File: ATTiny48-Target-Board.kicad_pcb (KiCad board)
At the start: 2 copper layers, 25.4 x 50.8 mm, 11 parts, among them J1 Conn_01x14_Pin, J2 Conn_01x14_Pin, U1 ATtiny48-P

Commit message: v1.0 ready to be paneled and sent to fab
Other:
- board text added: "/RST"
- board text added: "AVCC"
- board text added: "GND"
- board text added: "MISO"
- board text added: "MOSI"
- board text added: "PB0"
- board text added: "PB1"
- board text added: "PB2"
- board text added: "PB6"
- board text added: "PB7"
- board text added: "PC0"
- board text added: "PC1"
- board text added: "PC2"
- board text added: "PC3"
- board text added: "PC7"
- board text added: "PD0"
- board text added: "PD1"
- board text added: "PD2"
- board text added: "PD3"
- board text added: "PD4"
- board text added: "PD5"
- board text added: "RX"
- board text added: "SCK"
- board text added: "SCL"
- board text added: "SDA"
- board text added: "TX"
- board text added: "VCC"
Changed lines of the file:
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@@
     (title "ATtiny48 Target Board")
     (date "2023-06-13")
-    (rev "v0.4")
+    (rev "v1.0")
+    (comment 1 "Bare Bones MicroController for ATtiny48 & ATtiny88")
+    (comment 2 "BBMC-T48/T88")
   )
   (layers
@@
   (gr_rect (start 107.95 44.196) (end 133.35 94.996)
     (stroke (width 0.15) (type default)) (fill none) (layer "Edge.Cuts"))
-  (gr_text "BBMC-T48/T88\nV1.0   N7TDB" (at 114.808 57.404 90) (layer "F.SilkS")
-    (effects (font (size 1 1) (thickness 0.15)) (justify left bottom))
-  )
+  (gr_text "GND" (at 127.254 60.96) (layer "F.SilkS")
+    (effects (font (size 1 1) (thickness 0.15)) (justify left bottom))
+  )
+  (gr_text "BBMC-T48/T88\nV1.0   N7TDB" (at 115.57 94.234 90) (layer "F.SilkS")
+    (effects (font (size 0.8 0.7) (thickness 0.125)) (justify left bottom))
+  )
+  (gr_text "PB6" (at 110.744 66.04) (layer "F.SilkS")
+    (effects (font (size 1 1) (thickness 0.15)) (justify left bottom))
+  )
+  (gr_text "PC0" (at 127.254 58.42) (layer "F.SilkS")
+    (effects (font (size 1 1) (thickness 0.15)) (justify left bottom))
+  )
+  (gr_text "SCK" (at 127.254 68.58) (layer "F.SilkS")
+    (effects (font (size 1 1) (thickness 0.15)) (justify left bottom))
+  )
+  (gr_text "PB1" (at 127.254 78.74) (layer "F.SilkS")
+    (effects (font (size 1 1) (thickness 0.15)) (justify left bottom))
+  )
+  (gr_text "PC3" (at 127.254 50.8) (layer "F.SilkS")
+    (effects (font (size 1 1) (thickness 0.15)) (justify left bottom))
+  )
+  (gr_text "AVCC" (at 126.492 66.04) (layer "F.SilkS")
+    (effects (font (size 1 1) (thickness 0.15)) (justify left bottom))
+  )
+  (gr_text "GND" (at 110.55 63.53) (layer "F.SilkS")
+    (effects (font (size 1 1) (thickness 0.15)) (justify left bottom))
+  )
+  (gr_text "SDA" (at 127.254 48.26) (layer "F.SilkS")
+    (effects (font (size 1 1) (thickness 0.15)) (justify left bottom))
+  )
+  (gr_text "PB2" (at 127.254 76.2) (layer "F.SilkS")
+    (effects (font (size 1 1) (thickness 0.15)) (justify left bottom))
+  )
+  (gr_text "TX" (at 110.744 73.66) (layer "F.SilkS")
+    (effects (font (size 1 1) (thickness 0.15)) (justify left bottom))
+  )
+  (gr_text "PD4" (at 110.744 58.42) (layer "F.SilkS")
+    (effects (font (size 1 1) (thickness 0.15)) (justify left bottom))
+  )
+  (gr_text "PB0" (at 110.744 78.74) (layer "F.SilkS")
+    (effects (font (size 1 1) (thickness 0.15)) (justify left bottom))
+  )
+  (gr_text "PC2" (at 127.254 53.34) (layer "F.SilkS")
+    (effects (font (size 1 1) (thickness 0.15)) (justify left bottom))
+  )
+  (gr_text "PD3" (at 110.744 55.88) (layer "F.SilkS")
+    (effects (font (size 1 1) (thickness 0.15)) (justify left bottom))
+  )
+  (gr_text "PB7" (at 110.744 68.58) (layer "F.SilkS")
+    (effects (font (size 1 1) (thickness 0.15)) (justify left bottom))
+  )
+  (gr_text "MOSI" (at 126.746 73.66) (layer "F.SilkS")
+    (effects (font (size 1 1) (thickness 0.15)) (justify left bottom))
+  )
+  (gr_text "PD0" (at 110.744 48.26) (layer "F.SilkS")
+    (effects (font (size 1 1) (thickness 0.15)) (justify left bottom))
+  )
+  (gr_text "PD1" (at 110.744 50.8) (layer "F.SilkS")
+    (effects (font (size 1 1) (thickness 0.15)) (justify left bottom))
+  )
+  (gr_text "PC7" (at 127.254 63.754) (layer "F.SilkS")
+    (effects (font (size 1 1) (thickness 0.15)) (justify left bottom))
+  )
+  (gr_text "PD5" (at 110.744 71.12) (layer "F.SilkS")
+    (effects (font (size 1 1) (thickness 0.15)) (justify left bottom))
+  )
+  (gr_text "RX" (at 110.744 76.2) (layer "F.SilkS")
+    (effects (font (size 1 1) (thickness 0.15)) (justify left bottom))
+  )
+  (gr_text "VCC" (at 110.744 60.96) (layer "F.SilkS")
+    (effects (font (size 1 1) (thickness 0.15)) (justify left bottom))
+  )
+  (gr_text "/RST" (at 110.744 45.72) (layer "F.SilkS")
+    (effects (font (size 1 1) (thickness 0.15)) (justify left bottom))
+  )
+  (gr_text "PC1" (at 127.254 55.88) (layer "F.SilkS")
+    (effects (font (size 1 1) (thickness 0.15)) (justify left bottom))
+  )
+  (gr_text "PD2" (at 110.744 53.34) (layer "F.SilkS")
+    (effects (font (size 1 1) (thickness 0.15)) (justify left bottom))
+  )
+  (gr_text "SCL" (at 127.254 45.72) (layer "F.SilkS")
+    (effects (font (size 1 1) (thickness 0.15)) (justify left bottom))
+  )
+  (gr_text "MISO" (at 126.746 71.12) (layer "F.SilkS")
+    (effects (font (size 1 1) (thickness 0.15)) (justify left bottom))
+  )

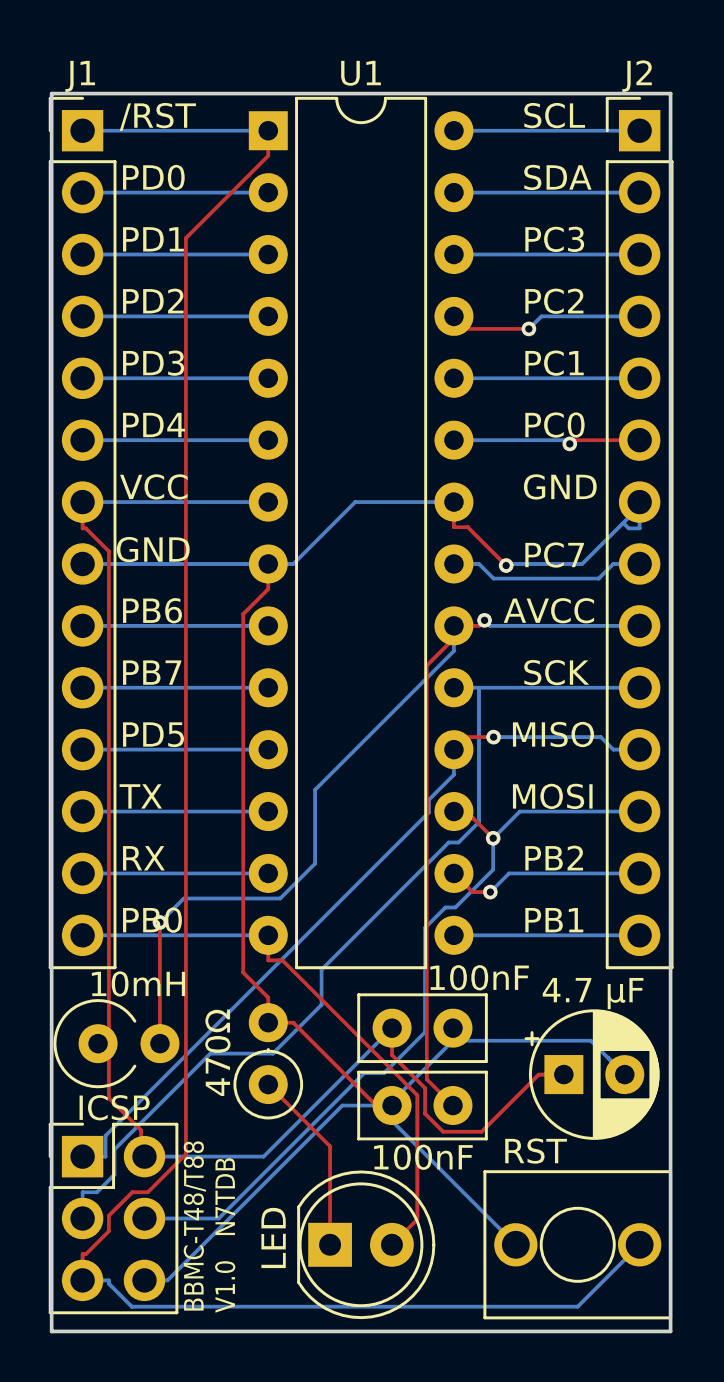
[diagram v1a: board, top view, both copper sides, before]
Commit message: v1.1 change hinky trace on pin 22
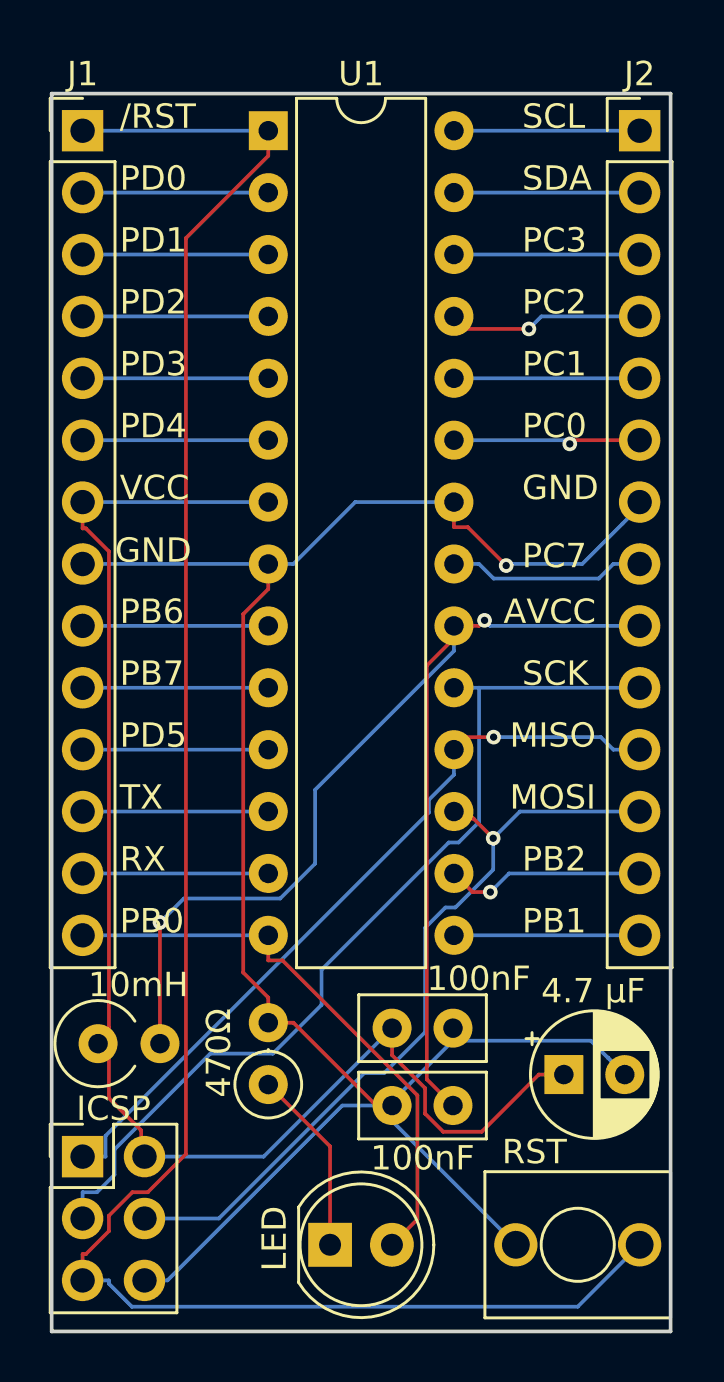
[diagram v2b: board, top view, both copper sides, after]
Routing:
- net GND: track 88.0 -> 86.1 mm
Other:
- board text added: "BBMC-T48/T88 V1.1 N7TDB"
- board text removed: "BBMC-T48/T88 V1.0 N7TDB"
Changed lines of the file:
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@@
   (title_block
     (title "ATtiny48 Target Board")
-    (date "2023-06-13")
-    (rev "v1.0")
+    (date "2023-06-14")
+    (rev "v1.1")
     (comment 1 "Bare Bones MicroController for ATtiny48 & ATtiny88")
     (comment 2 "BBMC-T48/T88")
@@
   )
   (setup
+    (stackup
+      (layer "F.SilkS" (type "Top Silk Screen"))
+      (layer "F.Paste" (type "Top Solder Paste"))
+      (layer "F.Mask" (type "Top Solder Mask") (thickness 0.01))
+      (layer "F.Cu" (type "copper") (thickness 0.035))
+      (layer "dielectric 1" (type "core") (thickness 1.51) (material "FR4") (epsilon_r 4.5) (loss_tangent 0.02))
+      (layer "B.Cu" (type "copper") (thickness 0.035))
+      (layer "B.Mask" (type "Bottom Solder Mask") (thickness 0.01))
+      (layer "B.Paste" (type "Bottom Solder Paste"))
+      (layer "B.SilkS" (type "Bottom Silk Screen"))
+      (copper_finish "None")
+      (dielectric_constraints no)
+    )
     (pad_to_mask_clearance 0.0508)
     (solder_mask_min_width 0.25)
@@
   (gr_rect (start 107.95 44.196) (end 133.35 94.996)
     (stroke (width 0.15) (type default)) (fill none) (layer "Edge.Cuts"))
+  (gr_text "BBMC-T48/T88\nV1.1   N7TDB" (at 114.808 46.99 90) (layer "B.SilkS")
+    (effects (font (size 1 1) (thickness 0.125)) (justify left bottom mirror))
+  )
   (gr_text "GND" (at 127.254 60.96) (layer "F.SilkS")
     (effects (font (size 1 1) (thickness 0.15)) (justify left bottom))
-  )
-  (gr_text "BBMC-T48/T88\nV1.0   N7TDB" (at 115.57 94.234 90) (layer "F.SilkS")
-    (effects (font (size 0.8 0.7) (thickness 0.125)) (justify left bottom))
   )
   (gr_text "PB6" (at 110.744 66.04) (layer "F.SilkS")
@@
   (via (at 126.603 63.5648) (size 0.6) (drill 0.3) (layers "F.Cu" "B.Cu") (net 15))
   (segment (start 116.84 63.5) (end 117.869 63.5) (width 0.1524) (layer "B.Cu") (net 15))
-  (segment (start 131.633 62.0387) (end 132.08 62.0387) (width 0.1524) (layer "B.Cu") (net 15))
   (segment (start 131.47 84.455) (end 131.4699 84.455) (width 0.1524) (layer "B.Cu") (net 15))
   (segment (start 121.92 85.5644) (end 124.42 83.0644) (width 0.1524) (layer "B.Cu") (net 15))
   (segment (start 130.774 83.7597) (end 130.775 83.7597) (width 0.1524) (layer "B.Cu") (net 15))
   (segment (start 111.76 92.9013) (end 112.701 92.9013) (width 0.1524) (layer "B.Cu") (net 15))
-  (segment (start 132.08 62.0387) (end 132.08 60.96) (width 0.1524) (layer "B.Cu") (net 15))
   (segment (start 131.377 61.8459) (end 131.8 61.4234) (width 0.1524) (layer "B.Cu") (net 15))
   (segment (start 112.701 92.9013) (end 119.877 85.725) (width 0.1524) (layer "B.Cu") (net 15))
@@
   (segment (start 121.92 85.725) (end 121.92 85.5644) (width 0.1524) (layer "B.Cu") (net 15))
   (segment (start 129.723 63.5) (end 131.377 61.8459) (width 0.1524) (layer "B.Cu") (net 15))
-  (segment (start 131.44 61.8459) (end 131.633 62.0387) (width 0.1524) (layer "B.Cu") (net 15))
   (segment (start 116.84 63.5) (end 109.22 63.5) (width 0.1524) (layer "B.Cu") (net 15))
   (segment (start 131.4699 84.455) (end 130.774 83.7597) (width 0.1524) (layer "B.Cu") (net 15))
@@
   (segment (start 130.079 83.0644) (end 130.774 83.7597) (width 0.1524) (layer "B.Cu") (net 15))
   (segment (start 124.42 83.0644) (end 124.42 82.55) (width 0.1524) (layer "B.Cu") (net 15))
-  (segment (start 131.377 61.8459) (end 131.44 61.8459) (width 0.1524) (layer "B.Cu") (net 15))
   (segment (start 126.603 63.5648) (end 126.668 63.5) (width 0.1524) (layer "B.Cu") (net 15))
   (segment (start 120.409 60.96) (end 124.46 60.96) (width 0.1524) (layer "B.Cu") (net 15))

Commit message: Still v1.1, but I dropped the panels.  This is the version sent to PCBWAY (again). mv gerbers.zip to panel-gerbers.zip generate gerber.zip from UNpaneled version
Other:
- rule pad_to_mask_clearance: 0.0508 -> 0
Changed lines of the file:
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@@
       (dielectric_constraints no)
     )
-    (pad_to_mask_clearance 0.0508)
-    (solder_mask_min_width 0.25)
+    (pad_to_mask_clearance 0)
     (pcbplotparams
       (layerselection 0x00010fc_ffffffff)
@@
       (outputformat 1)
       (mirror false)
-      (drillshape 1)
+      (drillshape 0)
       (scaleselection 1)
-      (outputdirectory "")
+      (outputdirectory "gerbers/")
     )
   )

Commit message: v1.2 sent to PCBWAY
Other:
- board text added: "BBMC-T48/T88 V1.2 N7TDB"
- board text removed: "BBMC-T48/T88 V1.1 N7TDB"
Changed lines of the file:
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@@
     (title "ATtiny48 Target Board")
     (date "2023-06-14")
-    (rev "v1.1")
+    (rev "v1.2")
     (comment 1 "Bare Bones MicroController for ATtiny48 & ATtiny88")
     (comment 2 "BBMC-T48/T88")
@@
   (gr_rect (start 107.95 44.196) (end 133.35 94.996)
     (stroke (width 0.15) (type default)) (fill none) (layer "Edge.Cuts"))
-  (gr_text "BBMC-T48/T88\nV1.1   N7TDB" (at 114.808 46.99 90) (layer "B.SilkS")
+  (gr_text "BBMC-T48/T88\nV1.2   N7TDB" (at 114.808 46.99 90) (layer "B.SilkS")
     (effects (font (size 1 1) (thickness 0.125)) (justify left bottom mirror))
   )
